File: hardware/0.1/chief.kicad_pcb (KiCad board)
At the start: 2 copper layers, 84.3 x 65 mm, 21 parts, among them SW1 Encoder_MX_RGB, SW10 Encoder_MX_RGB, SW11 MX_RGB, SW12 MX_RGB, SW2 MX_RGB, SW3 MX_RGB, SW4 Encoder_MX_RGB, SW5 MX_RGB, SW6 MX_RGB, SW7 Encoder_MX_RGB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

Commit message: parts ready to layout
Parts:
- removed LOGO1: Josh-Details, josh-logos:josh-details
- removed LOGO2: OSHW_FMask, josh-logos:OSHW_Logo_3.6x3.6_F.Mask
- removed LOGO3: Board-Title, josh-logos:board-title
- removed LOGO4: Josh-Logo, josh-logos:josh-johnson-logo-8_6x1_5
- removed LOGO5: 4-Layer-Check, josh-logos:4-layer-check
- added BZ1: Buzzer, Buzzer_Beeper:Buzzer_Murata_PKMCS0909E4000-R1, B.Cu at (127.3, 148.4)
- added C1: 1u, Capacitor_SMD:C_0603_1608Metric, B.Cu at (156.3, 140.6)
- added C10: 100n, Capacitor_SMD:C_0603_1608Metric, B.Cu at (160.3, 144.9)
- added C11: 100n, Capacitor_SMD:C_0603_1608Metric, B.Cu at (143.9, 133.2)
- added C12: 100n, Capacitor_SMD:C_0603_1608Metric, B.Cu at (148.2, 138.5)
- added C13: 100n, Capacitor_SMD:C_0603_1608Metric, B.Cu at (127.6, 130.5)
- added C14: 100n, Capacitor_SMD:C_0603_1608Metric, B.Cu at (152.3, 143.0)
- added C15: 100n, Capacitor_SMD:C_0603_1608Metric, B.Cu at (135.3, 97.9)
- added C2: 1u, Capacitor_SMD:C_0603_1608Metric, B.Cu at (163.6, 146.8)
- added C3: 10u, Capacitor_SMD:C_0603_1608Metric, B.Cu at (148.2, 133.4)
- added C4: 4u7, Capacitor_SMD:C_0603_1608Metric, B.Cu at (152.2, 138.0)
- added C5: 10u, Capacitor_SMD:C_0603_1608Metric, B.Cu at (159.0, 147.4)
- added C6: 100n, Capacitor_SMD:C_0603_1608Metric, B.Cu at (143.9, 130.7)
- added C7: 100n, Capacitor_SMD:C_0603_1608Metric, B.Cu at (156.3, 143.1)
- added C8: 100n, Capacitor_SMD:C_0603_1608Metric, B.Cu at (152.3, 140.5)
- added C9: 100n, Capacitor_SMD:C_0603_1608Metric, B.Cu at (148.2, 136.0)
- added D1: 1N4148, Diode_SMD:D_SOD-123, B.Cu at (147.1, 152.0)
- added D2: LED, LED_SMD:LED_0603_1608Metric, B.Cu at (123.6, 130.5)
- added F1: 500mA, josh-passives-smt:Fuse_0603_1608Metric, B.Cu at (161.0, 152.4)
- added FB1: 600R, josh-passives-smt:Ferrite_Bead_0603, B.Cu at (156.2, 135.5)
- added J1: USB_C_Receptacle_USB2.0, josh-connectors:USB_C_U262-161N-4BVC11, B.Cu at (142.8, 62.8)
- added JP1: Jumper_NC_Small, Jumper:SolderJumper-2_P1.3mm_Bridged_RoundedPad1.0x1.5mm, B.Cu at (144.1, 136.3)
- added Q1: DTC123J, Package_TO_SOT_SMD:SOT-23, B.Cu at (154.8, 146.7)
- added Q2: BSS138, Package_TO_SOT_SMD:SOT-23, B.Cu at (148.1, 142.0)
- added R1: 2K2, Resistor_SMD:R_0603_1608Metric, B.Cu at (152.2, 133.0)
- added R2: 100K, Resistor_SMD:R_0603_1608Metric, B.Cu at (160.3, 142.4)
- added R3: 10K, Resistor_SMD:R_0603_1608Metric, B.Cu at (156.0, 137.3)
- added R4: 10K, Resistor_SMD:R_0603_1608Metric, B.Cu at (157.0, 153.1)
- added R5: 2K2, Resistor_SMD:R_0603_1608Metric, B.Cu at (152.2, 135.5)
- added RN1: 10K, Resistor_SMD:R_Array_Convex_4x0603, B.Cu at (139.8, 133.9)
- added RN2: 10K, Resistor_SMD:R_Array_Convex_4x0603, B.Cu at (150.5, 146.7)
- added RN3: 10K, Resistor_SMD:R_Array_Convex_4x0603, B.Cu at (146.3, 147.9)
- added RN4: 10K, Resistor_SMD:R_Array_Convex_4x0603, B.Cu at (157.0, 150.5)
- added RN5: 5K1, Resistor_SMD:R_Array_Convex_4x0603, B.Cu at (143.8, 140.4)
- added SW13: SW_Push, josh-buttons-switches:Panasonic_EVQPUL_EVQPUC, B.Cu at (137.3, 139.0)
- added U1: AP2112K-3.3, Package_TO_SOT_SMD:SOT-23-5, B.Cu at (152.4, 151.3)
- added U2: USBLC6-2SC6, Package_TO_SOT_SMD:SOT-23-6, B.Cu at (142.8, 70.3)
- added U3: STM32F072C8Tx, Package_QFP:LQFP-48_7x7mm_P0.5mm, B.Cu at (142.9, 100.0)
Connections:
- net Net-(SW1-PadS1) renamed /SW1
- net Net-(SW10-PadS1) renamed /SW10
- net Net-(SW4-PadS1) renamed /SW4
- net Net-(SW7-PadS1) renamed /SW7
- SW1 pad 1: (no net) -> /LED_dat
- SW1 pad 2: (no net) -> Net-(SW1-Pad2)
- SW1 pad 3: (no net) -> +5V
- SW1 pad 4: (no net) -> GND
- SW1 pad A: (no net) -> /ENC1A
- SW1 pad B: (no net) -> /ENC1B
- SW1 pad C: (no net) -> GND
- SW1 pad S2: Net-(SW1-PadS2) -> GND
- SW10 pad 1: (no net) -> Net-(SW10-Pad1)
- SW10 pad 2: (no net) -> /LED1
- SW10 pad 3: (no net) -> +5V
- SW10 pad 4: (no net) -> GND
- SW10 pad A: (no net) -> /ENC4A
- SW10 pad B: (no net) -> /ENC4B
- SW10 pad C: (no net) -> GND
- SW10 pad S2: Net-(SW10-PadS2) -> GND
- SW11 pad 2: (no net) -> GND
- SW11 pad 3: (no net) -> Net-(SW11-Pad3)
- SW11 pad 4: (no net) -> /LED2
- SW11 pad 5: (no net) -> +5V
- SW11 pad 6: (no net) -> GND
- SW12 pad 2: (no net) -> GND
- SW12 pad 3: (no net) -> Net-(SW12-Pad3)
- SW12 pad 5: (no net) -> +5V
- SW12 pad 6: (no net) -> GND
- SW2 pad 2: (no net) -> GND
- SW2 pad 3: (no net) -> /LED1
- SW2 pad 4: (no net) -> Net-(SW2-Pad4)
- SW2 pad 5: (no net) -> +5V
- SW2 pad 6: (no net) -> GND
- SW3 pad 2: (no net) -> GND
- SW3 pad 3: (no net) -> /LED2
- SW3 pad 4: (no net) -> Net-(SW3-Pad4)
- SW3 pad 5: (no net) -> +5V
- SW3 pad 6: (no net) -> GND
- SW4 pad 1: (no net) -> Net-(SW1-Pad2)
- SW4 pad 2: (no net) -> Net-(SW4-Pad2)
- SW4 pad 3: (no net) -> +5V
- SW4 pad 4: (no net) -> GND
- SW4 pad A: (no net) -> /ENC2A
- SW4 pad B: (no net) -> /ENC2B
- SW4 pad C: (no net) -> GND
- SW4 pad S2: Net-(SW4-PadS2) -> GND
- SW5 pad 2: (no net) -> GND
- SW5 pad 3: (no net) -> Net-(SW2-Pad4)
- SW5 pad 4: (no net) -> Net-(SW5-Pad4)
- SW5 pad 5: (no net) -> +5V
- SW5 pad 6: (no net) -> GND
- SW6 pad 2: (no net) -> GND
- SW6 pad 3: (no net) -> Net-(SW3-Pad4)
- SW6 pad 4: (no net) -> Net-(SW6-Pad4)
- SW6 pad 5: (no net) -> +5V
- SW6 pad 6: (no net) -> GND
- SW7 pad 1: (no net) -> Net-(SW4-Pad2)
- SW7 pad 2: (no net) -> Net-(SW10-Pad1)
- SW7 pad 3: (no net) -> +5V
- SW7 pad 4: (no net) -> GND
- SW7 pad A: (no net) -> /ENC3A
- SW7 pad B: (no net) -> /ENC3B
- SW7 pad C: (no net) -> GND
- SW7 pad S2: Net-(SW7-PadS2) -> GND
- SW8 pad 2: (no net) -> GND
- SW8 pad 3: (no net) -> Net-(SW5-Pad4)
- SW8 pad 4: (no net) -> Net-(SW11-Pad3)
- SW8 pad 5: (no net) -> +5V
- SW8 pad 6: (no net) -> GND
- SW9 pad 2: (no net) -> GND
- SW9 pad 3: (no net) -> Net-(SW6-Pad4)
- SW9 pad 4: (no net) -> Net-(SW12-Pad3)
- SW9 pad 5: (no net) -> +5V
- SW9 pad 6: (no net) -> GND
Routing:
- net +3V3: track 0.00 -> 2.92 mm

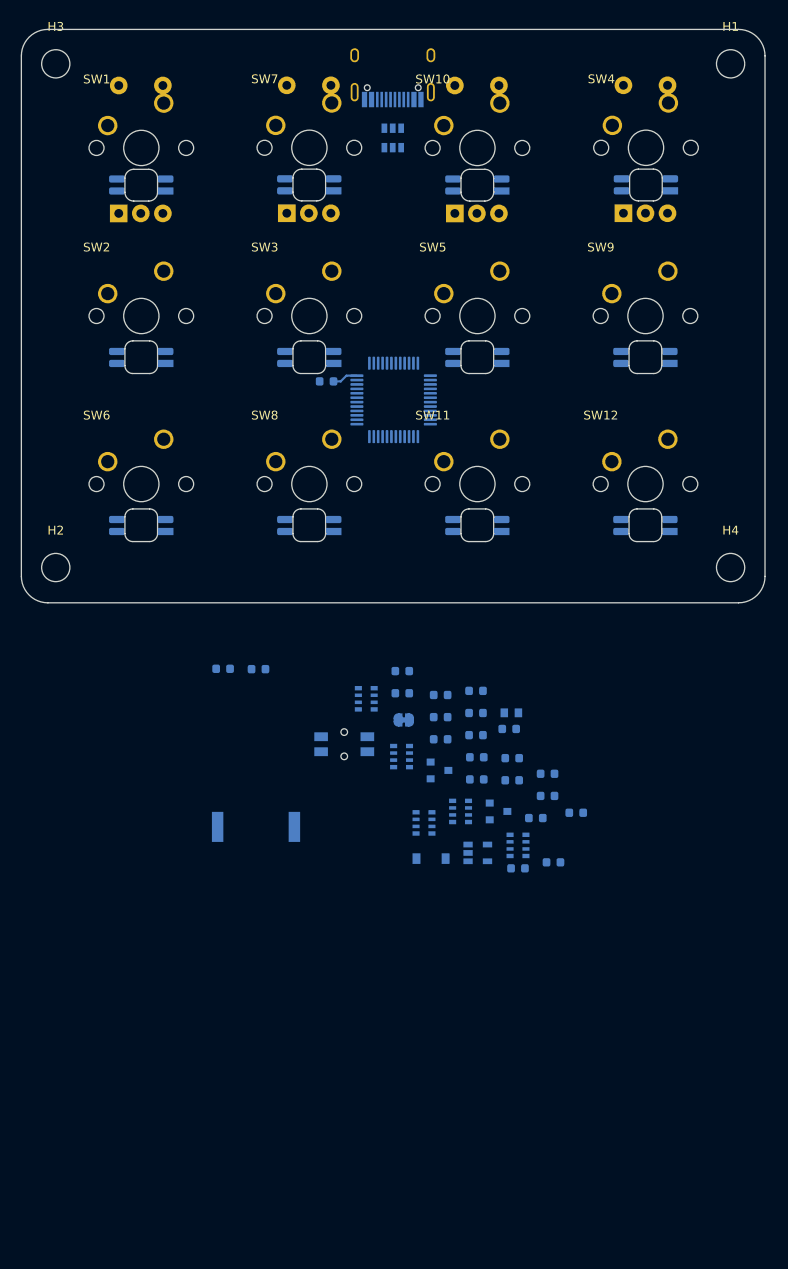
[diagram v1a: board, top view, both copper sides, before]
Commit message: Layout complete. ENC2/ENC2DB swapped with ENC3/ENC3DB to match resistor labelling
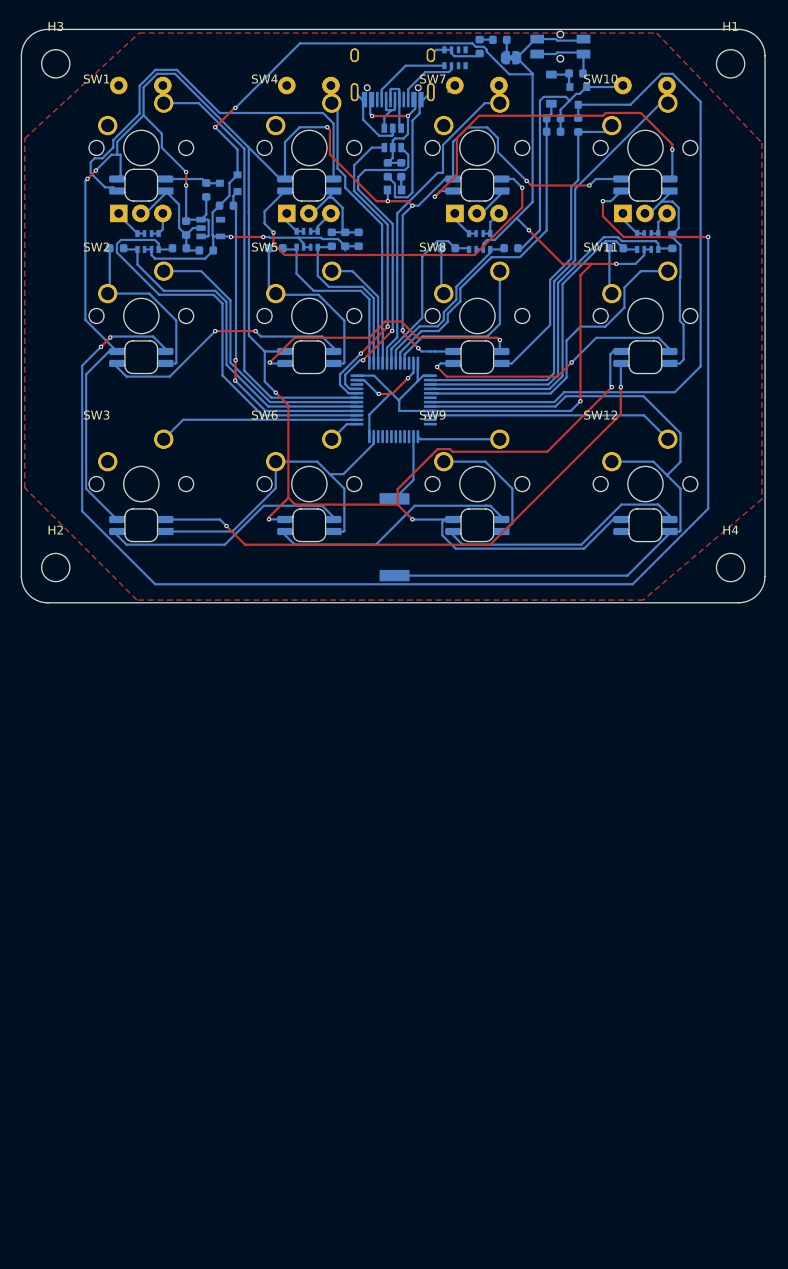
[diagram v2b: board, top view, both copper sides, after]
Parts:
- moved D1 88.3 mm to (160.8, 64.8), turned to 90 degrees
- moved R4 84.6 mm to (121.7, 76.2), turned to 90 degrees
- moved SW13 82.8 mm to (161.8, 59.9), turned to 180 degrees
- moved Q1 81.6 mm to (163.8, 65.5), turned to 270 degrees
- moved F1 80.4 mm to (143.8, 73.9), turned to 90 degrees
- moved RN5 79.4 mm to (149.9, 61.2), turned to 90 degrees
- moved C5 77.8 mm to (161.0, 69.6)
- moved U1 77.0 mm to (122.2, 80.5)
- moved R5 76.4 mm to (154.9, 59.2), turned to 180 degrees
- moved C2 76.3 mm to (121.7, 83.1), turned to 180 degrees
- moved D2 76.3 mm to (152.7, 59.9), turned to 90 degrees
- moved JP1 76.0 mm to (156.2, 61.2), turned to 180 degrees
- moved C10 74.8 mm to (118.6, 82.8)
- moved R2 74.3 mm to (161.0, 68.1)
- moved R1 70.9 mm to (163.6, 63.0)
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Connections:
- J1 pad A8: (no net) -> Net-(J1-PadA8)
- J1 pad B8: (no net) -> Net-(J1-PadB8)
- RN1 pad 1: /ENC1B -> /ENC1B_DB
- RN1 pad 2: /ENC1A -> +3V3
- RN1 pad 4: +3V3 -> /ENC1A_DB
- RN1 pad 5: /ENC1B -> /ENC1A
- RN1 pad 7: /ENC1A_DB -> /ENC1B
- RN1 pad 8: /ENC1B_DB -> /ENC1B
- RN2 pad 1: /ENC3B -> /ENC2B_DB
- RN2 pad 2: /ENC3A -> +3V3
- RN2 pad 4: +3V3 -> /ENC2A_DB
- RN2 pad 5: /ENC3B -> /ENC2A
- RN2 pad 6: /ENC3A -> /ENC2A
- RN2 pad 7: /ENC3A_DB -> /ENC2B
- RN2 pad 8: /ENC3B_DB -> /ENC2B
- RN3 pad 1: /ENC2B -> /ENC3B_DB
- RN3 pad 2: /ENC2A -> +3V3
- RN3 pad 4: +3V3 -> /ENC3A_DB
- RN3 pad 5: /ENC2B -> /ENC3A
- RN3 pad 6: /ENC2A -> /ENC3A
- RN3 pad 7: /ENC2A_DB -> /ENC3B
- RN3 pad 8: /ENC2B_DB -> /ENC3B
- RN4 pad 1: /ENC4B -> /ENC4B_DB
- RN4 pad 2: /ENC4A -> +3V3
- RN4 pad 4: +3V3 -> /ENC4A_DB
- RN4 pad 5: /ENC4B -> /ENC4A
- RN4 pad 7: /ENC4A_DB -> /ENC4B
- RN4 pad 8: /ENC4B_DB -> /ENC4B
- RN5 pad 4: GND -> Net-(J1-PadA5)
- RN5 pad 5: Net-(J1-PadA5) -> GND
- SW11 pad 1: (no net) -> /SW11
- SW12 pad 1: (no net) -> /SW12
- SW12 pad 4: (no net) -> Net-(SW12-Pad4)
- SW2 pad 1: (no net) -> /SW2
- SW3 pad 1: (no net) -> /SW3
- SW5 pad 1: (no net) -> /SW5
- SW6 pad 1: (no net) -> /SW6
- SW8 pad 1: (no net) -> /SW8
- SW9 pad 1: (no net) -> /SW9
- U1 pad 4: (no net) -> Net-(U1-Pad4)
- U3 pad 10: (no net) -> /SW12
- U3 pad 11: (no net) -> Net-(U3-Pad11)
- U3 pad 12: (no net) -> Net-(U3-Pad12)
- U3 pad 13: (no net) -> /SW9
- U3 pad 15: (no net) -> Net-(U3-Pad15)
- U3 pad 16: (no net) -> Net-(U3-Pad16)
- U3 pad 17: (no net) -> Net-(U3-Pad17)
- U3 pad 18: (no net) -> Net-(U3-Pad18)
- U3 pad 19: (no net) -> Net-(U3-Pad19)
- U3 pad 2: (no net) -> /SW10
- U3 pad 20: (no net) -> Net-(U3-Pad20)
- U3 pad 21: (no net) -> Net-(U3-Pad21)
- U3 pad 22: (no net) -> Net-(U3-Pad22)
- U3 pad 25: (no net) -> /SW6
- U3 pad 26: (no net) -> /SW3
- U3 pad 27: (no net) -> /ENC1B_DB
- U3 pad 29: (no net) -> /ENC1A_DB
- U3 pad 3: (no net) -> /ENC4B_DB
- U3 pad 30: (no net) -> /SW2
- U3 pad 31: (no net) -> /SW1
- U3 pad 34: (no net) -> Net-(U3-Pad34)
- U3 pad 37: (no net) -> /ENC2A_DB
- U3 pad 38: (no net) -> /ENC2B_DB
- U3 pad 39: (no net) -> /SW5
- U3 pad 4: (no net) -> /ENC4A_DB
- U3 pad 40: (no net) -> /SW4
- U3 pad 41: (no net) -> /SW7
- U3 pad 42: (no net) -> /ENC3A_DB
- U3 pad 43: (no net) -> /ENC3B_DB
- U3 pad 45: (no net) -> /SW8
- U3 pad 46: (no net) -> Net-(U3-Pad46)
- U3 pad 5: (no net) -> /SW11
- U3 pad 6: (no net) -> Net-(U3-Pad6)
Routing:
- net GND: track 0.00 -> 357.8 mm, vias 0 -> 2
- net +5V: track 0.00 -> 315.7 mm, vias 0 -> 15
- net +3V3: track 2.92 -> 196.6 mm, vias 0 -> 7
- net /LED1: track 0.00 -> 154.5 mm, vias 0 -> 4
- net /nRST: track 0.00 -> 80.5 mm
- net /LED2: track 0.00 -> 64.7 mm, vias 0 -> 2
- net /SW10: track 0.00 -> 53.6 mm
- net /SW1: track 0.00 -> 52.8 mm
- net Net-(SW1-Pad2): track 0.00 -> 48.1 mm
- net /ENC1B_DB: track 0.00 -> 48.0 mm
- net Net-(SW4-Pad2): track 0.00 -> 43.3 mm, vias 0 -> 2
- net /ENC4B_DB: track 0.00 -> 41.6 mm
- net Net-(SW10-Pad1): track 0.00 -> 41.1 mm, vias 0 -> 2
- net /BOOT0: track 0.00 -> 40.3 mm
- net /SW7: track 0.00 -> 39.1 mm
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- added copper zone on F.Cu, net GND

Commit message: delete Bing's hard work
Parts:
- moved C15 26.7 mm to (146.3, 106.9), turned to 270 degrees
- moved C14 16.6 mm to (135.2, 98.0), turned to 180 degrees
- moved RN5 10.1 mm to (157.8, 67.5), turned to 180 degrees
- moved D1 9.65 mm to (160.6, 74.4)
- moved Q1 9.65 mm to (163.6, 75.2)
- moved R1 9.65 mm to (163.4, 72.6)
- moved C4 9.65 mm to (163.6, 78.5)
- moved C5 9.65 mm to (160.8, 79.2)
- moved R2 9.65 mm to (160.8, 77.7)
- moved JP1 9.58 mm to (162.8, 68.2)
- moved R5 9.58 mm to (161.5, 66.1)
- moved C2 4.02 mm to (124.9, 80.7), turned to 90 degrees
- moved C3 3.95 mm to (138.3, 74.6)
- moved F1 3.95 mm to (139.9, 74.6)
- moved FB1 3.95 mm to (139.1, 76.8)
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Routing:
- net GND: track 357.8 -> 8.58 mm, vias 2 -> 0
- net +5V: track 315.7 -> 1.35 mm, vias 15 -> 0
- net +3V3: track 196.6 -> 0.00 mm, vias 7 -> 0
- net /LED1: track 154.5 -> 0.00 mm, vias 4 -> 0
- net /nRST: track 80.5 -> 1.51 mm
- net /LED2: track 64.7 -> 0.00 mm, vias 2 -> 0
- net /SW10: track 53.6 -> 0.00 mm
- net /SW1: track 52.8 -> 0.00 mm
- net Net-(SW1-Pad2): track 48.1 -> 0.00 mm
- net /ENC1B_DB: track 48.0 -> 0.00 mm
- net Net-(SW4-Pad2): track 43.3 -> 0.00 mm, vias 2 -> 0
- net /ENC4B_DB: track 41.6 -> 0.00 mm
- net Net-(SW10-Pad1): track 41.1 -> 0.00 mm, vias 2 -> 0
- net /SW7: track 39.1 -> 0.00 mm
- net /ENC1A_DB: track 39.0 -> 0.00 mm
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
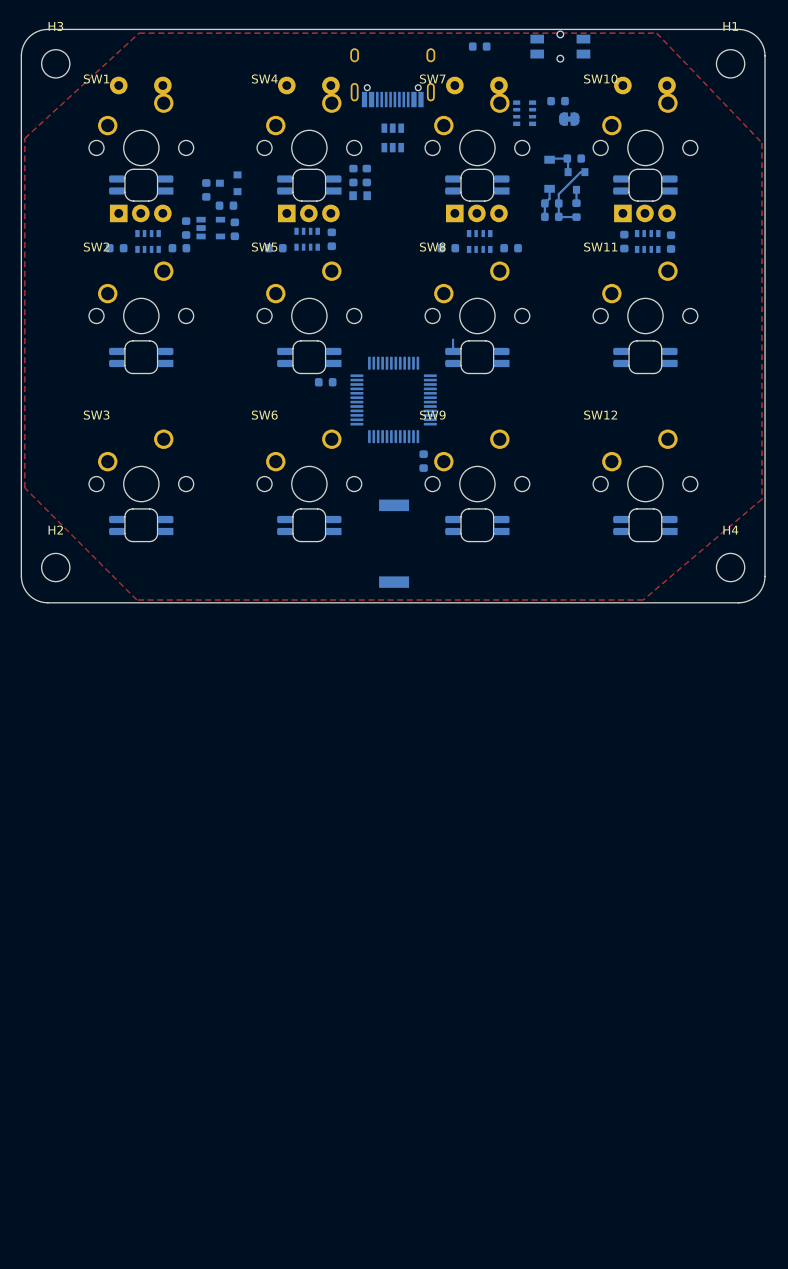
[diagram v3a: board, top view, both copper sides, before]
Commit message: Footprints arranged and layout attempted
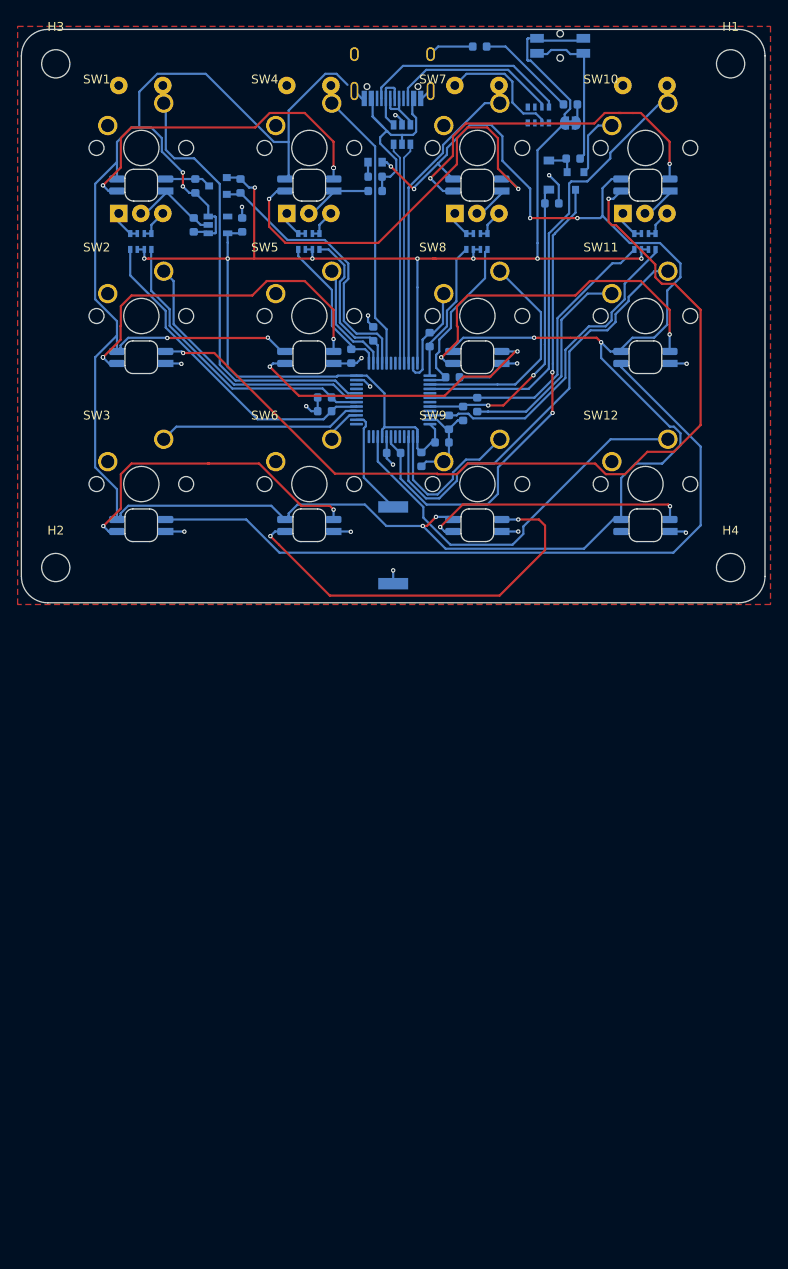
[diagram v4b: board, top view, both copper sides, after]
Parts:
- moved C4 34.5 mm to (142.9, 106.0), turned to 180 degrees
- moved C13 32.4 mm to (149.2, 102.5), turned to 270 degrees
- moved C6 30.0 mm to (135.1, 101.3)
- moved C9 24.9 mm to (152.4, 100.5), turned to 270 degrees
- moved C5 24.5 mm to (150.8, 101.5), turned to 270 degrees
- moved C10 23.6 mm to (135.1, 99.7), turned to 180 degrees
- moved C12 16.1 mm to (149.6, 97.4)
- moved C7 14.9 mm to (138.1, 95.0), turned to 270 degrees
- moved C14 14.8 mm to (148.4, 104.8), turned to 0 degrees
- moved C11 11.7 mm to (140.6, 92.5)
- moved C8 10.6 mm to (147.0, 93.2), turned to 90 degrees
- moved FB1 4.16 mm to (140.8, 73.0), turned to 180 degrees
- moved C3 3.03 mm to (140.8, 76.3), turned to 180 degrees
- moved R3 2.74 mm to (125.5, 75.7), turned to 270 degrees
- moved RN5 1.57 mm to (159.3, 67.7), turned to 270 degrees
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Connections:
- U3 pad 13: /SW9 -> Net-(U3-Pad13)
- U3 pad 15: Net-(U3-Pad15) -> /SW6
- U3 pad 16: Net-(U3-Pad16) -> /SW3
- U3 pad 17: Net-(U3-Pad17) -> /ENC1A_DB
- U3 pad 18: Net-(U3-Pad18) -> /ENC1B_DB
- U3 pad 19: Net-(U3-Pad19) -> /SW2
- U3 pad 2: /SW10 -> /SW9
- U3 pad 20: Net-(U3-Pad20) -> /SW1
- U3 pad 25: /SW6 -> /ENC2A_DB
- U3 pad 26: /SW3 -> /SW5
- U3 pad 27: /ENC1B_DB -> /ENC2B_DB
- U3 pad 29: /ENC1A_DB -> /SW4
- U3 pad 3: /ENC4B_DB -> /SW11
- U3 pad 30: /SW2 -> Net-(U3-Pad30)
- U3 pad 31: /SW1 -> Net-(U3-Pad31)
- U3 pad 34: Net-(U3-Pad34) -> /SW7
- U3 pad 37: /ENC2A_DB -> /ENC3A_DB
- U3 pad 38: /ENC2B_DB -> /ENC3B_DB
- U3 pad 39: /SW5 -> /SW8
- U3 pad 4: /ENC4A_DB -> Net-(U3-Pad4)
- U3 pad 40: /SW4 -> /SW10
- U3 pad 41: /SW7 -> Net-(U3-Pad41)
- U3 pad 42: /ENC3A_DB -> /ENC4A_DB
- U3 pad 43: /ENC3B_DB -> Net-(U3-Pad43)
- U3 pad 45: /SW8 -> Net-(U3-Pad45)
- U3 pad 46: Net-(U3-Pad46) -> /ENC4B_DB
- U3 pad 5: /SW11 -> Net-(U3-Pad5)
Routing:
- net +5V: track 1.35 -> 324.2 mm, vias 0 -> 12
- net +3V3: track 0.00 -> 174.8 mm, vias 0 -> 8
- net GND: track 8.58 -> 147.0 mm, vias 0 -> 16
- net /LED1: track 0.00 -> 102.6 mm, vias 0 -> 2
- net /LED2: track 0.00 -> 86.2 mm
- net /nRST: track 1.51 -> 56.1 mm, vias 0 -> 2
- net /SW10: track 0.00 -> 53.8 mm
- net /SW1: track 0.00 -> 52.5 mm
- net /SW11: track 0.00 -> 49.6 mm
- net Net-(SW4-Pad2): track 0.00 -> 48.8 mm, vias 0 -> 2
- net Net-(SW6-Pad4): track 0.00 -> 45.9 mm, vias 0 -> 2
- net /SW12: track 0.00 -> 45.8 mm
- net Net-(SW10-Pad1): track 0.00 -> 40.8 mm, vias 0 -> 2
- net Net-(SW2-Pad4): track 0.00 -> 40.1 mm, vias 0 -> 3
- net Net-(SW1-Pad2): track 0.00 -> 39.9 mm, vias 0 -> 4
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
